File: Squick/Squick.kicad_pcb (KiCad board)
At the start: 2 copper layers, 92 x 92 mm, 103 parts, among them J1 BT, J10 D24V3F-5V, J2 DEBUG_UART, J3 PROG, J4 VL53L0X_L, J5 VL53L0X_F, J6 VL53L0X_R, J7 ENK_L, J8 ENK_R, J9 BATT, Q1 AO3407A, Q2 AO3407A, SW1 USER_BUT_1, SW2 USER_BUT_2, SW3 RESET, SW4 ON/OFF, T1 SFH-313FA, T2 SFH-313FA, T3 SFH-313FA, T4 SFH-313FA, T5 SFH-313FA, T6 SFH-313FA, U1 STM32F411RETx, U10 LM1117-3.3, U2 CD4051B, U3 KTIR0711S, U4 CD4051B, U5 KTIR0711S, U6 KTIR0711S, U7 KTIR0711S, U8 Adafruit_4554, U9 TB6612FNG

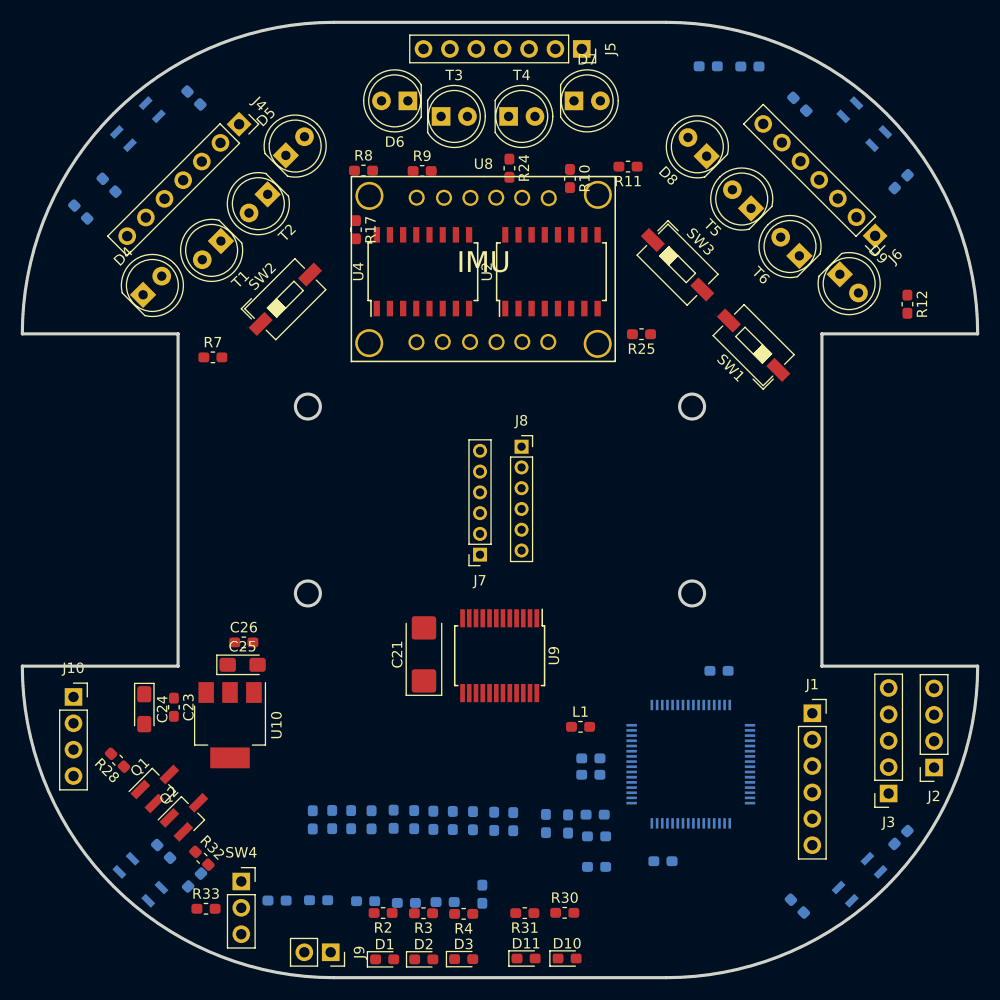
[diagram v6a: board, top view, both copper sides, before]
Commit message: Started connecting pads
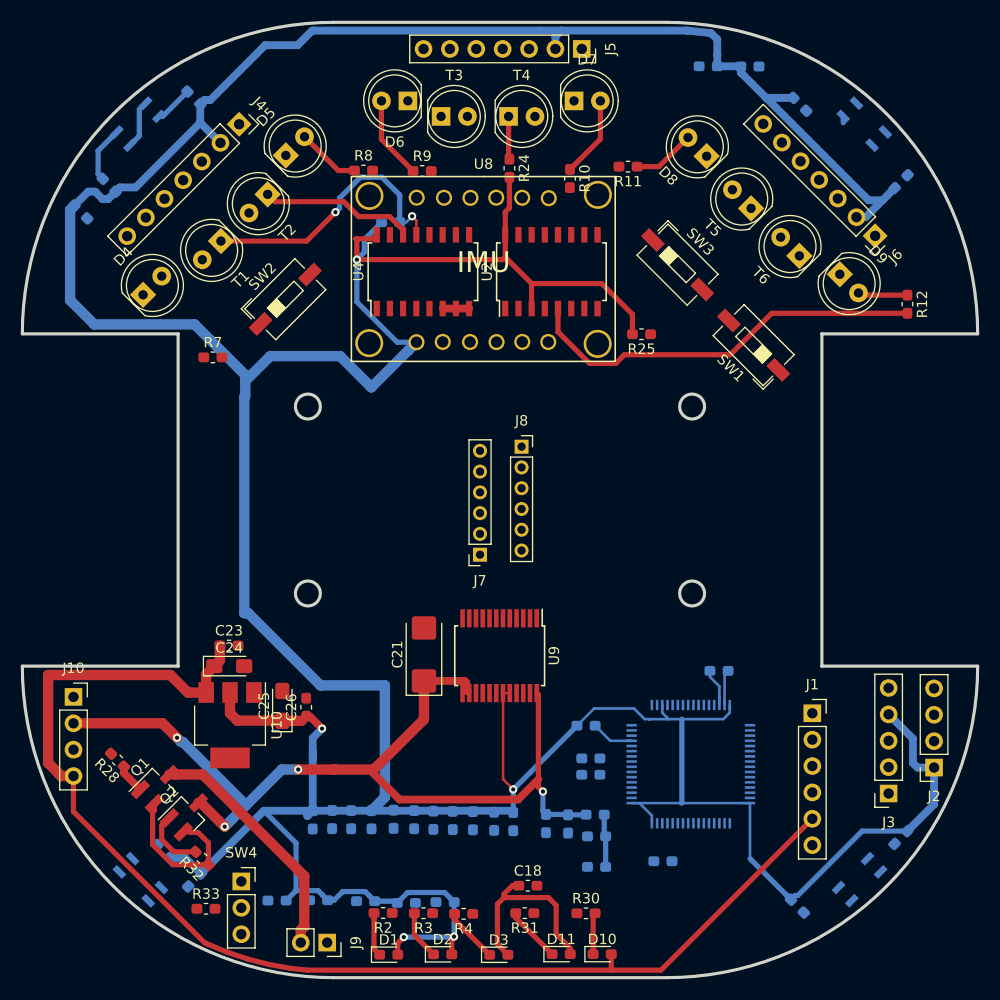
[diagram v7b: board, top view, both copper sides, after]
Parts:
- C18: moved to F.Cu
- L1, R17: moved to B.Cu
- moved C24 9.17 mm to (154.0, 95.9), turned to 0 degrees
- moved C26 8.66 mm to (161.5, 99.9), turned to 90 degrees
- moved C23 7.97 mm to (154.0, 94.0), turned to 0 degrees
- moved C25 5.50 mm to (159.2, 99.8), turned to 90 degrees
- moved C18 4.46 mm to (182.8, 117.1), turned to 0 degrees
- moved R17 3.42 mm to (169.6, 53.2), turned to 180 degrees
- moved D10 3.41 mm to (190.0, 123.7)
- moved D11 3.41 mm to (186.0, 123.7)
- moved D3 3.41 mm to (180.0, 123.7)
- moved R30 2.05 mm to (188.4, 119.7)
- moved D2 1.88 mm to (174.6, 123.7)
- moved J9 0.99 mm to (163.5, 122.6)
- moved D1 0.60 mm to (169.4, 123.7)
- moved L1 0.54 mm to (188.4, 101.7)
- turned R32 to 135 degrees
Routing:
- net +3.3V: track 0.00 -> 488.7 mm, vias 0 -> 5
- net +5V: track 0.00 -> 120.6 mm
- net Vin: track 0.00 -> 89.9 mm, vias 0 -> 4
- net IR_6: track 0.00 -> 39.6 mm
- net PT_1: track 0.00 -> 27.1 mm, vias 0 -> 2
- net VCC: track 0.00 -> 23.6 mm
- net Net-(Q1-Pad2): track 0.00 -> 15.1 mm
- net PT_2: track 0.00 -> 14.9 mm
- net GND: track 0.00 -> 14.1 mm
- net Net-(D6-Pad2): track 0.00 -> 8.01 mm
- net Net-(D7-Pad2): track 0.00 -> 7.81 mm
- net Net-(D5-Pad2): track 0.00 -> 6.16 mm
- net Net-(Q2-Pad1): track 0.00 -> 6.14 mm
- net Net-(D8-Pad2): track 0.00 -> 6.06 mm
- net Net-(R13-Pad2): track 0.00 -> 5.43 mm
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
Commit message: Connecting is not funny anymore
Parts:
- C2, C8, R5: moved to F.Cu
- moved R5 34.1 mm to (199.8, 108.5), turned to 90 degrees
- moved C2 8.47 mm to (201.5, 108.5), turned to 270 degrees
- moved C10 5.51 mm to (170.3, 115.6)
- moved C14 5.51 mm to (183.9, 115.8)
- moved C15 5.51 mm to (164.6, 115.6)
- moved C16 5.51 mm to (180.1, 115.7)
- moved C17 5.51 mm to (182.1, 115.8)
- moved C19 5.51 mm to (187.1, 116.0)
- moved C20 5.51 mm to (189.2, 116.0)
- moved C22 5.51 mm to (192.0, 120.2)
- moved C4 5.51 mm to (166.5, 115.6)
- moved C6 5.51 mm to (174.4, 115.6)
- moved C7 5.51 mm to (168.3, 115.6)
- moved C9 5.51 mm to (178.1, 115.7)
- moved R29 5.51 mm to (192.0, 117.2)
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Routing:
- net RESET: track 0.00 -> 95.2 mm, vias 0 -> 6
- net KTIR_3: track 0.00 -> 77.6 mm, vias 0 -> 2
- net BUT_1: track 0.00 -> 61.4 mm, vias 0 -> 3
- net +5V: track 120.6 -> 167.3 mm
- net L_IN2: track 0.00 -> 40.5 mm, vias 0 -> 1
- net PWM_L: track 0.00 -> 39.7 mm, vias 0 -> 1
- net R_IN1: track 0.00 -> 37.7 mm, vias 0 -> 1
- net L_IN1: track 0.00 -> 37.0 mm, vias 0 -> 1
- net R_IN2: track 0.00 -> 34.0 mm, vias 0 -> 1
- net PWM_R: track 0.00 -> 30.2 mm, vias 0 -> 1
- net BT_TX: track 0.00 -> 26.9 mm, vias 0 -> 1
- net DEBUG_RX: track 0.00 -> 25.9 mm, vias 0 -> 1
- net PT_6: track 0.00 -> 25.3 mm, vias 0 -> 1
- net +3.3V: track 488.7 -> 512.5 mm, vias 5 -> 8
- net BT_RX: track 0.00 -> 22.7 mm, vias 0 -> 1
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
